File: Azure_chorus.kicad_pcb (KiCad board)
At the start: 2 copper layers, 51 x 68 mm, 90 parts, among them Q1 2N5088, Q2 2N5088, Q3 2N5088, Q4 2N5088, Q5 2N5088, SW1 SW_DPDT_x2, U1 RC4558, U2 MN3207, U3 MN3102, U4 TL022

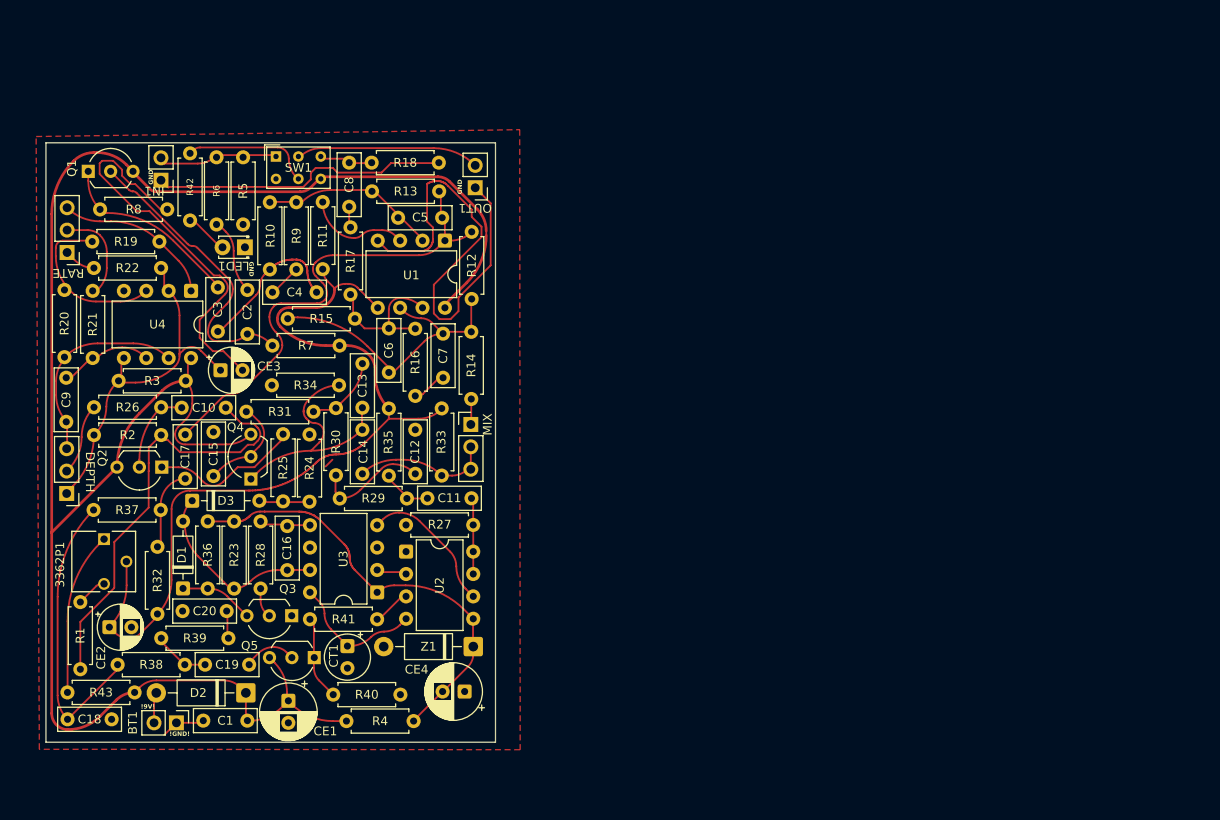
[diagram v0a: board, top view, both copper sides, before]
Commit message: Major UPD
Schem: remade bypass, added switch to vibrato mode;

PCB: deleted old PCB, and placed firs components on new;

other: created Pr_Lib and .gitignore.
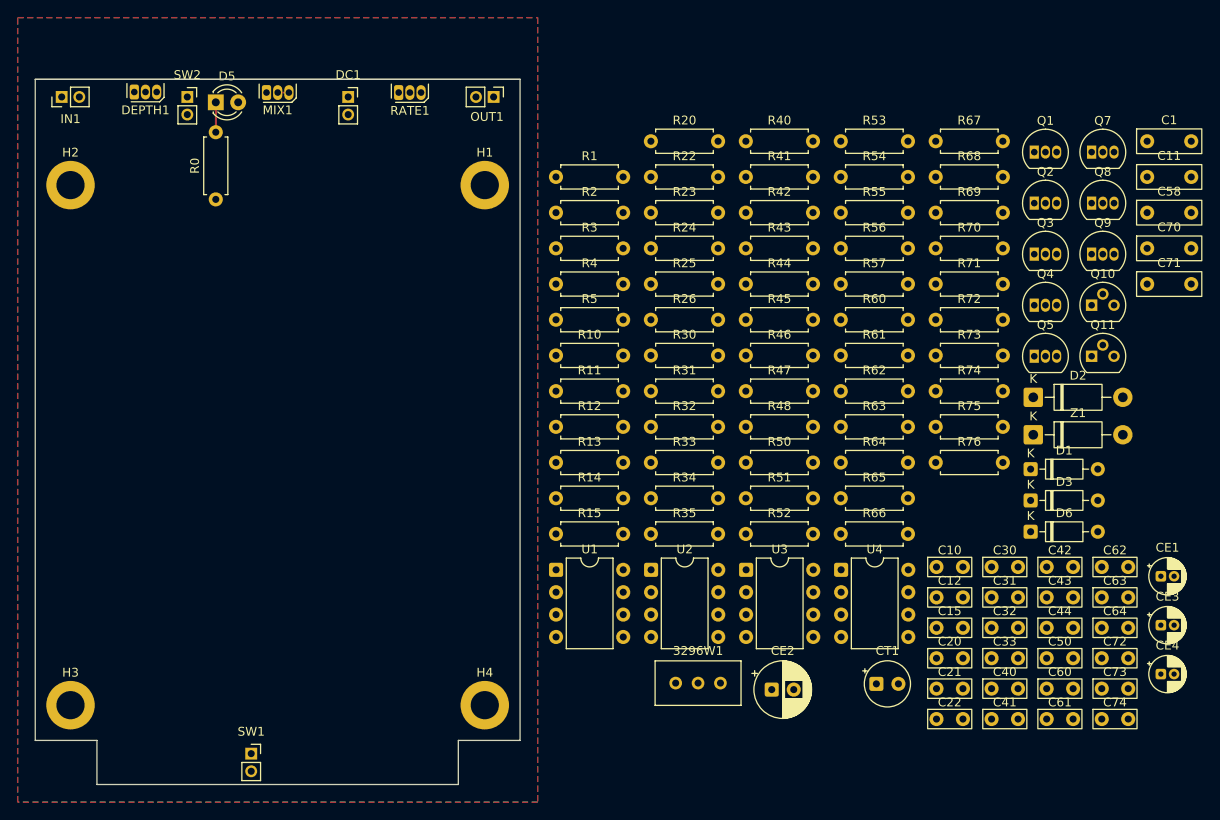
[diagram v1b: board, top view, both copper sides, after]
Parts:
- removed 3362P1: 10K, MY_LIBA:POT_3362P
- removed BT1: CRONA, Connector_PinHeader_2.54mm:PinHeader_1x02_P2.54mm_Vertical
- removed C13: 8n2, Capacitor_THT:C_Disc_D7.0mm_W2.5mm_P5.00mm
- removed C14, C17: 33n, Capacitor_THT:C_Disc_D7.0mm_W2.5mm_P5.00mm
- removed C16: 47p, Capacitor_THT:C_Disc_D7.0mm_W2.5mm_P5.00mm
- removed C18: 3n3, Capacitor_THT:C_Disc_D7.0mm_W2.5mm_P5.00mm
- removed C19: 8n3, Capacitor_THT:C_Disc_D7.0mm_W2.5mm_P5.00mm
- removed C2: 47n, Capacitor_THT:C_Disc_D7.0mm_W2.5mm_P5.00mm
- removed C3: 470n, Capacitor_THT:C_Disc_D7.0mm_W2.5mm_P5.00mm
- removed C4, C7: 6n8, Capacitor_THT:C_Disc_D7.0mm_W2.5mm_P5.00mm
- removed C5, C6: 100p, Capacitor_THT:C_Disc_D7.0mm_W2.5mm_P5.00mm
- removed C8: 1u, Capacitor_THT:C_Disc_D7.0mm_W2.5mm_P5.00mm
- removed C9: 100n, Capacitor_THT:C_Disc_D7.0mm_W2.5mm_P5.00mm
- removed DEPTH, RATE: 100KB, Connector_PinHeader_2.54mm:PinHeader_1x03_P2.54mm_Vertical
- removed LED1: LED, LED_THT:LED_D1.8mm_W3.3mm_H2.4mm
- removed MIX: 250kC, Connector_PinHeader_2.54mm:PinHeader_1x03_P2.54mm_Vertical
- removed R16, R29, R37, R38, R39, R8, R9: 10K, Resistor_THT:R_Axial_DIN0207_L6.3mm_D2.5mm_P7.62mm_Horizontal
- removed R17: 470R, Resistor_THT:R_Axial_DIN0207_L6.3mm_D2.5mm_P7.62mm_Horizontal
- removed R18: 100K, Resistor_THT:R_Axial_DIN0207_L6.3mm_D2.5mm_P7.62mm_Horizontal
- removed R19: 47M, Resistor_THT:R_Axial_DIN0207_L6.3mm_D2.5mm_P7.62mm_Horizontal
- removed R21: 1M, Resistor_THT:R_Axial_DIN0207_L6.3mm_D2.5mm_P7.62mm_Horizontal
- removed R27: 56K, Resistor_THT:R_Axial_DIN0207_L6.3mm_D2.5mm_P7.62mm_Horizontal
- removed R28: 33K, Resistor_THT:R_Axial_DIN0207_L6.3mm_D2.5mm_P7.62mm_Horizontal
- removed R36: 2K7, Resistor_THT:R_Axial_DIN0207_L6.3mm_D2.5mm_P7.62mm_Horizontal
- removed R6: 1K, Resistor_THT:R_Axial_DIN0207_L6.3mm_D2.5mm_P7.62mm_Horizontal
- removed R7: 470K, Resistor_THT:R_Axial_DIN0207_L6.3mm_D2.5mm_P7.62mm_Horizontal
- added 3296W1: 10K, Potentiometer_THT:Potentiometer_Bourns_3296W_Vertical, F.Cu at (157.7, 128.5)
- added C21: 100p, Pr_Lib:C_Disc_D4.3_W1.9_P5.00, F.Cu at (182.2, 129.1)
- added C22: 6n8, Pr_Lib:C_Disc_D4.3_W1.9_P5.00, F.Cu at (182.2, 132.6)
- added C30: 33n, Pr_Lib:C_Disc_D4.3_W1.9_P5.00, F.Cu at (188.5, 115.3)
- added C31: 3n3, Pr_Lib:C_Disc_D4.3_W1.9_P5.00, F.Cu at (188.5, 118.8)
- added C32: 8n3, Pr_Lib:C_Disc_D4.3_W1.9_P5.00, F.Cu at (188.5, 122.2)
- added C33: 470p, Pr_Lib:C_Disc_D4.3_W1.9_P5.00, F.Cu at (188.5, 125.7)
- added C40: 47p, Pr_Lib:C_Disc_D4.3_W1.9_P5.00, F.Cu at (188.5, 129.1)
- added C41: 33n, Pr_Lib:C_Disc_D4.3_W1.9_P5.00, F.Cu at (188.5, 132.6)
- added C42: 2n2, Pr_Lib:C_Disc_D4.3_W1.9_P5.00, F.Cu at (194.7, 115.3)
- added C43: 8n2, Pr_Lib:C_Disc_D4.3_W1.9_P5.00, F.Cu at (194.7, 118.8)
- added C44: 33n, Pr_Lib:C_Disc_D4.3_W1.9_P5.00, F.Cu at (194.7, 122.2)
- added C50: 10n, Pr_Lib:C_Disc_D4.3_W1.9_P5.00, F.Cu at (194.7, 125.7)
- added C58: 100n, Pr_Lib:C_disc_D7_W2.5_P5, F.Cu at (206.1, 75.1)
- added C60: 1n, Pr_Lib:C_Disc_D4.3_W1.9_P5.00, F.Cu at (194.7, 129.1)
- added C61: 1n, Pr_Lib:C_Disc_D4.3_W1.9_P5.00, F.Cu at (194.7, 132.6)
- added C62: 1n, Pr_Lib:C_Disc_D4.3_W1.9_P5.00, F.Cu at (201.0, 115.3)
- added C63: 1n, Pr_Lib:C_Disc_D4.3_W1.9_P5.00, F.Cu at (201.0, 118.8)
- added C64: 1n, Pr_Lib:C_Disc_D4.3_W1.9_P5.00, F.Cu at (201.0, 122.2)
- added C70: 100n, Pr_Lib:C_disc_D7_W2.5_P5, F.Cu at (206.1, 79.2)
- added C71: 100n, Pr_Lib:C_disc_D7_W2.5_P5, F.Cu at (206.1, 83.2)
- added C72: 1u, Pr_Lib:C_Disc_D4.3_W1.9_P5.00, F.Cu at (201.0, 125.7)
- added C73: 10n, Pr_Lib:C_Disc_D4.3_W1.9_P5.00, F.Cu at (201.0, 129.1)
- added C74: 10n, Pr_Lib:C_Disc_D4.3_W1.9_P5.00, F.Cu at (201.0, 132.6)
- added D5: LED, LED_THT:LED_D3.0mm, F.Cu at (100.5, 62.6)
- added D6: 1N914, Diode_THT:D_DO-35_SOD27_P7.62mm_Horizontal, F.Cu at (192.9, 111.3)
- added DC1: DC, Connector_PinSocket_2.00mm:PinSocket_1x02_P2.00mm_Vertical, F.Cu at (115.5, 62.0)
- added DEPTH1: 100KB, Package_TO_SOT_THT:TO-92S, F.Cu at (91.2, 61.4)
- added H1: MountingHole_Pad, MountingHole:MountingHole_3.2mm_M3_ISO14580_Pad, F.Cu at (131.0, 72.0)
- added H2: MountingHole_Pad, MountingHole:MountingHole_3.2mm_M3_ISO14580_Pad, F.Cu at (84.0, 72.0)
- added H3: MountingHole_Pad, MountingHole:MountingHole_3.2mm_M3_ISO14580_Pad, F.Cu at (84.0, 131.0)
- added H4: MountingHole_Pad, MountingHole:MountingHole_3.2mm_M3_ISO14580_Pad, F.Cu at (131.0, 131.0)
- added MIX1: 250kC, Package_TO_SOT_THT:TO-92S, F.Cu at (106.2, 61.5)
- added Q10: J201, Package_TO_SOT_THT:TO-92, F.Cu at (199.8, 85.6)
- added Q11: J201, Package_TO_SOT_THT:TO-92, F.Cu at (199.8, 91.4)
- added Q7: 2SC1815, Package_TO_SOT_THT:TO-92_Inline, F.Cu at (199.8, 68.3)
- added Q8: 2SC1815, Package_TO_SOT_THT:TO-92_Inline, F.Cu at (199.8, 74.0)
- added Q9: 2SC1815, Package_TO_SOT_THT:TO-92_Inline, F.Cu at (199.8, 79.8)
- added R0: 3K, Resistor_THT:R_Axial_DIN0207_L6.3mm_D2.5mm_P7.62mm_Horizontal, F.Cu at (100.5, 73.6)
- added R44: 10K, Resistor_THT:R_Axial_DIN0207_L6.3mm_D2.5mm_P7.62mm_Horizontal, F.Cu at (160.6, 83.2)
- added R45: 10K, Resistor_THT:R_Axial_DIN0207_L6.3mm_D2.5mm_P7.62mm_Horizontal, F.Cu at (160.6, 87.3)
- added R46: 10K, Resistor_THT:R_Axial_DIN0207_L6.3mm_D2.5mm_P7.62mm_Horizontal, F.Cu at (160.6, 91.3)
- added R47: 10K, Resistor_THT:R_Axial_DIN0207_L6.3mm_D2.5mm_P7.62mm_Horizontal, F.Cu at (160.6, 95.4)
- added R48: 1M, Resistor_THT:R_Axial_DIN0207_L6.3mm_D2.5mm_P7.62mm_Horizontal, F.Cu at (160.6, 99.4)
- added R50: 150K, Resistor_THT:R_Axial_DIN0207_L6.3mm_D2.5mm_P7.62mm_Horizontal, F.Cu at (160.6, 103.5)
- added R51: 4K7, Resistor_THT:R_Axial_DIN0207_L6.3mm_D2.5mm_P7.62mm_Horizontal, F.Cu at (160.6, 107.5)
- added R52: 4K7, Resistor_THT:R_Axial_DIN0207_L6.3mm_D2.5mm_P7.62mm_Horizontal, F.Cu at (160.6, 111.6)
- added R53: 220K, Resistor_THT:R_Axial_DIN0207_L6.3mm_D2.5mm_P7.62mm_Horizontal, F.Cu at (171.4, 67.0)
- added R54: 33K, Resistor_THT:R_Axial_DIN0207_L6.3mm_D2.5mm_P7.62mm_Horizontal, F.Cu at (171.4, 71.1)
- added R55: 47M, Resistor_THT:R_Axial_DIN0207_L6.3mm_D2.5mm_P7.62mm_Horizontal, F.Cu at (171.4, 75.1)
- added R56: 10K, Resistor_THT:R_Axial_DIN0207_L6.3mm_D2.5mm_P7.62mm_Horizontal, F.Cu at (171.4, 79.2)
- added R57: 1M, Resistor_THT:R_Axial_DIN0207_L6.3mm_D2.5mm_P7.62mm_Horizontal, F.Cu at (171.4, 83.2)
- added R60: 62K, Resistor_THT:R_Axial_DIN0207_L6.3mm_D2.5mm_P7.62mm_Horizontal, F.Cu at (171.4, 87.3)
- added R61: 22K, Resistor_THT:R_Axial_DIN0207_L6.3mm_D2.5mm_P7.62mm_Horizontal, F.Cu at (171.4, 91.3)
- added R62: 1M, Resistor_THT:R_Axial_DIN0207_L6.3mm_D2.5mm_P7.62mm_Horizontal, F.Cu at (171.4, 95.4)
- added R63: 22R, Resistor_THT:R_Axial_DIN0207_L6.3mm_D2.5mm_P7.62mm_Horizontal, F.Cu at (171.4, 99.4)
- added R64: 56K, Resistor_THT:R_Axial_DIN0207_L6.3mm_D2.5mm_P7.62mm_Horizontal, F.Cu at (171.4, 103.5)
- added R65: 56K, Resistor_THT:R_Axial_DIN0207_L6.3mm_D2.5mm_P7.62mm_Horizontal, F.Cu at (171.4, 107.5)
- added R66: 10K, Resistor_THT:R_Axial_DIN0207_L6.3mm_D2.5mm_P7.62mm_Horizontal, F.Cu at (171.4, 111.6)
- added R67: 10K, Resistor_THT:R_Axial_DIN0207_L6.3mm_D2.5mm_P7.62mm_Horizontal, F.Cu at (182.2, 67.0)
- added R68: 1M, Resistor_THT:R_Axial_DIN0207_L6.3mm_D2.5mm_P7.62mm_Horizontal, F.Cu at (182.2, 71.1)
- added R69: 100R, Resistor_THT:R_Axial_DIN0207_L6.3mm_D2.5mm_P7.62mm_Horizontal, F.Cu at (182.2, 75.1)
- added R70: 470R, Resistor_THT:R_Axial_DIN0207_L6.3mm_D2.5mm_P7.62mm_Horizontal, F.Cu at (182.2, 79.2)
- added R71: 510K, Resistor_THT:R_Axial_DIN0207_L6.3mm_D2.5mm_P7.62mm_Horizontal, F.Cu at (182.2, 83.2)
- added R72: 510K, Resistor_THT:R_Axial_DIN0207_L6.3mm_D2.5mm_P7.62mm_Horizontal, F.Cu at (182.2, 87.3)
- added R73: 510K, Resistor_THT:R_Axial_DIN0207_L6.3mm_D2.5mm_P7.62mm_Horizontal, F.Cu at (182.2, 91.3)
- added R74: 100K, Resistor_THT:R_Axial_DIN0207_L6.3mm_D2.5mm_P7.62mm_Horizontal, F.Cu at (182.2, 95.4)
- added R75: 1M, Resistor_THT:R_Axial_DIN0207_L6.3mm_D2.5mm_P7.62mm_Horizontal, F.Cu at (182.2, 99.4)
- added R76: 1M, Resistor_THT:R_Axial_DIN0207_L6.3mm_D2.5mm_P7.62mm_Horizontal, F.Cu at (182.2, 103.5)
- added RATE1: 100KB, Package_TO_SOT_THT:TO-92S, F.Cu at (121.2, 61.5)
- added SW2: SW_SPST, Connector_PinSocket_2.00mm:PinSocket_1x02_P2.00mm_Vertical, F.Cu at (97.2, 62.0)
- C1: footprint Capacitor_THT:C_Disc_D7.0mm_W2.5mm_P5.00mm -> Pr_Lib:C_disc_D7_W2.5_P5
- C10: value 10n -> 47n; footprint Capacitor_THT:C_Disc_D7.0mm_W2.5mm_P5.00mm -> Pr_Lib:C_Disc_D4.3_W1.9_P5.00
- C11: value 33n -> 470n; footprint Capacitor_THT:C_Disc_D7.0mm_W2.5mm_P5.00mm -> Pr_Lib:C_disc_D7_W2.5_P5
- C12: value 2n2 -> 6n8; footprint Capacitor_THT:C_Disc_D7.0mm_W2.5mm_P5.00mm -> Pr_Lib:C_Disc_D4.3_W1.9_P5.00
- C15: footprint Capacitor_THT:C_Disc_D7.0mm_W2.5mm_P5.00mm -> Pr_Lib:C_Disc_D4.3_W1.9_P5.00
- C20: value 470p -> 100p; footprint Capacitor_THT:C_Disc_D7.0mm_W2.5mm_P5.00mm -> Pr_Lib:C_Disc_D4.3_W1.9_P5.00
- CE1: footprint Capacitor_THT:CP_Radial_D6.3mm_P2.50mm -> Capacitor_THT:CP_Radial_D4.0mm_P1.50mm
- CE2: value 47n -> 200u; footprint Capacitor_THT:CP_Radial_D5.0mm_P2.50mm -> Capacitor_THT:CP_Radial_D6.3mm_P2.50mm
- CE3: footprint Capacitor_THT:CP_Radial_D5.0mm_P2.50mm -> Capacitor_THT:CP_Radial_D4.0mm_P1.50mm
- CE4: value 200u -> 47n; footprint Capacitor_THT:CP_Radial_D6.3mm_P2.50mm -> Capacitor_THT:CP_Radial_D4.0mm_P1.50mm
- IN1, OUT1: footprint Connector_PinHeader_2.54mm:PinHeader_1x02_P2.54mm_Vertical -> Connector_PinHeader_2.00mm:PinHeader_1x02_P2.00mm_Vertical
- Q1, Q2, Q3, Q4, Q5: footprint Package_TO_SOT_THT:TO-92_Inline_Wide -> Package_TO_SOT_THT:TO-92_Inline
- R1: value 4K7 -> 33R
- R10: value 47K -> 2M2
- R11: value 10K -> 1K
- R12: value 47K -> 470K
- R13, R15: value 47K -> 10K
- R20: value 33K -> 10K
- R22: value 10K -> 47K
- R23: value 150K -> 47K
- R24, R25: value 4K7 -> 47K
- R26: value 220K -> 10K
- R30: value 10K -> 100K
- R32: value 100K -> 10K
- R33: value 1M -> 10K
- R35: value 300K -> 4K7
- R4: value 33R -> 4K7
- R40: value 10K -> 2K7
- R41: value 4K7 -> 33K
- R42: value 10K -> 56K
- R43: value 4K7 -> 300K
- R5: value 2M2 -> 4K7
- SW1: value SW_DPDT_x2 -> SW_Push; footprint Button_Switch_THT:SW_NKK_GW12LJP -> Connector_PinSocket_2.00mm:PinSocket_1x02_P2.00mm_Vertical
- moved C1 121.4 mm to (206.1, 67.0), turned to 0 degrees
- moved CE3 110.5 mm to (207.7, 121.9)
- moved Q1 107.3 mm to (193.3, 68.3)
- moved Q2 103.4 mm to (193.3, 74.0), turned to 0 degrees
- moved CE1 100.0 mm to (207.7, 116.4), turned to 0 degrees
- moved D1 97.1 mm to (192.9, 104.2), turned to 0 degrees
- moved D2 95.4 mm to (193.2, 96.1), turned to 0 degrees
- moved D3 95.1 mm to (192.9, 107.8)
- moved Q3 93.7 mm to (193.3, 79.8), turned to 0 degrees
- moved R43 92.0 mm to (160.6, 79.2)
- moved Q4 91.0 mm to (193.3, 85.6), turned to 0 degrees
- moved C11 89.4 mm to (206.1, 71.1)
- moved Q5 88.5 mm to (193.3, 91.4), turned to 0 degrees
- moved C10 87.5 mm to (182.2, 115.3)
- moved C20 85.7 mm to (182.2, 125.7)
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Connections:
- C10 pad 1: Net-(Q2-B) -> Net-(C10-Pad1)
- C10 pad 2: GND -> /Q1_B
- C11 pad 1: Net-(C11-Pad1) -> Net-(Q1-E)
- C11 pad 2: /U2_OUT -> Net-(C11-Pad2)
- C12 pad 1: Net-(C12-Pad1) -> Net-(C11-Pad2)
- C12 pad 2: GND -> Net-(C12-Pad2)
- C20 pad 1: GND -> /PR_IN
- C20 pad 2: Net-(C20-Pad2) -> /RC_OUT
- CE2 pad 1: /VB -> GND
- CE2 pad 2: GND -> /VD
- CE4 pad 1: GND -> /VB
- CE4 pad 2: /VD -> GND
- D2 pad 2: Net-(D2-A) -> +9V
- OUT1 pad 2: Net-(SW1A-B) -> /OUTPUT
- R1 pad 1: Net-(3362P1-Pad3) -> /VD
- R1 pad 2: GND -> /VA
- R10 pad 1: Net-(C3-Pad2) -> /IN
- R10 pad 2: /PR_IN -> GND
- R11 pad 1: /VB -> /IN
- R11 pad 2: Net-(U1A-+) -> Net-(C10-Pad1)
- R12 pad 1: /RC_OUT -> /Q1_B
- R12 pad 2: /U1_6 -> /VB
- R13 pad 1: /RC_OUT -> GND
- R13 pad 2: /PR_IN -> Net-(Q1-E)
- R14 pad 1: /U1_6 -> Net-(C11-Pad2)
- R14 pad 2: Net-(MIX1-Pad1) -> /PR_IN
- R15 pad 1: /U1_7 -> Net-(C12-Pad2)
- R15 pad 2: /U1_6 -> /PR_IN
- R20 pad 1: Net-(U4A-+) -> /VB
- R20 pad 2: Net-(C9-Pad2) -> Net-(U1A-+)
- R22 pad 1: Net-(R22-Pad1) -> /RC_OUT
- R22 pad 2: /VC -> /PR_IN
- R23 pad 1: /LFO -> Net-(SW2-B)
- R23 pad 2: /VD -> /U1_6
- R24 pad 1: Net-(D3-A) -> /U1_6
- R24 pad 2: GND -> Net-(MIX1-Pad1)
- R25 pad 1: Net-(Q2-E) -> /OUT
- R25 pad 2: Net-(D3-A) -> /U1_6
- R26 pad 2: Net-(Q2-B) -> /OUT
- R30 pad 1: Net-(C13-Pad1) -> /VB
- R30 pad 2: Net-(C12-Pad1) -> Net-(C30-Pad2)
- R31 pad 1: Net-(Q4-B) -> Net-(C30-Pad2)
- R31 pad 2: Net-(C13-Pad1) -> Net-(C31-Pad2)
- R32 pad 1: /VB -> Net-(C31-Pad2)
- R32 pad 2: Net-(C17-Pad2) -> Net-(C32-Pad1)
- R33 pad 1: /RC_IN -> Net-(C32-Pad1)
- R33 pad 2: /VB -> Net-(C33-Pad2)
- R34 pad 1: /Q4_1 -> GND
- R34 pad 2: GND -> /Q5_1
- R35 pad 1: Net-(C11-Pad1) -> /Q5_1
- R35 pad 2: /VB -> /MN_IN
- R4 pad 1: /VD -> Net-(3296W1-Pad3)
- R4 pad 2: /VA -> GND
- R40 pad 1: GND -> /VD
- R40 pad 2: /Q5_1 -> Net-(D1-K)
- R41 pad 1: /Q5_1 -> Net-(Q3-B)
- R41 pad 2: /MN_IN -> Net-(U3-OX3)
- R42 pad 1: Net-(SW1B-B) -> /U2_OUT
- R42 pad 2: Net-(LED1-A) -> GND
- R43 pad 2: /VA -> /VB
- R5 pad 1: /IN -> Net-(3296W1-Pad1)
- R5 pad 2: GND -> /VA
- SW1 pad 1: /IN -> Net-(R62-Pad1)
- SW1 pad 2: Net-(SW1A-B) -> Net-(C60-Pad1)
- U1 pad 7: /U1_7 -> /OUT
- U4 pad 7: Net-(C9-Pad2) -> Net-(C58-Pad2)
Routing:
- net /VA: track 215.1 -> 0.00 mm
- net GND: track 191.7 -> 0.00 mm
- net /VB: track 98.8 -> 0.00 mm
- net /RC_OUT: track 55.9 -> 0.00 mm
- net /VD: track 50.9 -> 0.00 mm
- net /VC: track 42.0 -> 0.00 mm
- net /U1_6: track 34.6 -> 0.00 mm
- net /Q1_B: track 33.9 -> 0.00 mm
- net Net-(C18-Pad2): track 33.6 -> 0.00 mm
- net /Q4_1: track 28.1 -> 0.00 mm
- net Net-(C9-Pad2): track 23.5 -> 0.00 mm
- net /LFO: track 22.0 -> 0.00 mm
- net Net-(Q1-E): track 21.2 -> 0.00 mm
- net Net-(SW1A-B): track 20.8 -> 0.00 mm
- net /PR_IN: track 20.1 -> 0.00 mm
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- added copper zone on B.Cu, net GND
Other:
- board size 51 x 68 mm -> 55 x 80 mm
- board text removed: "!9V!"
- board text removed: "!GND!"
- board text removed: "GND"
